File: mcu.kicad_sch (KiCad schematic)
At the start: 1 part, among them U1 STM32H747IITx

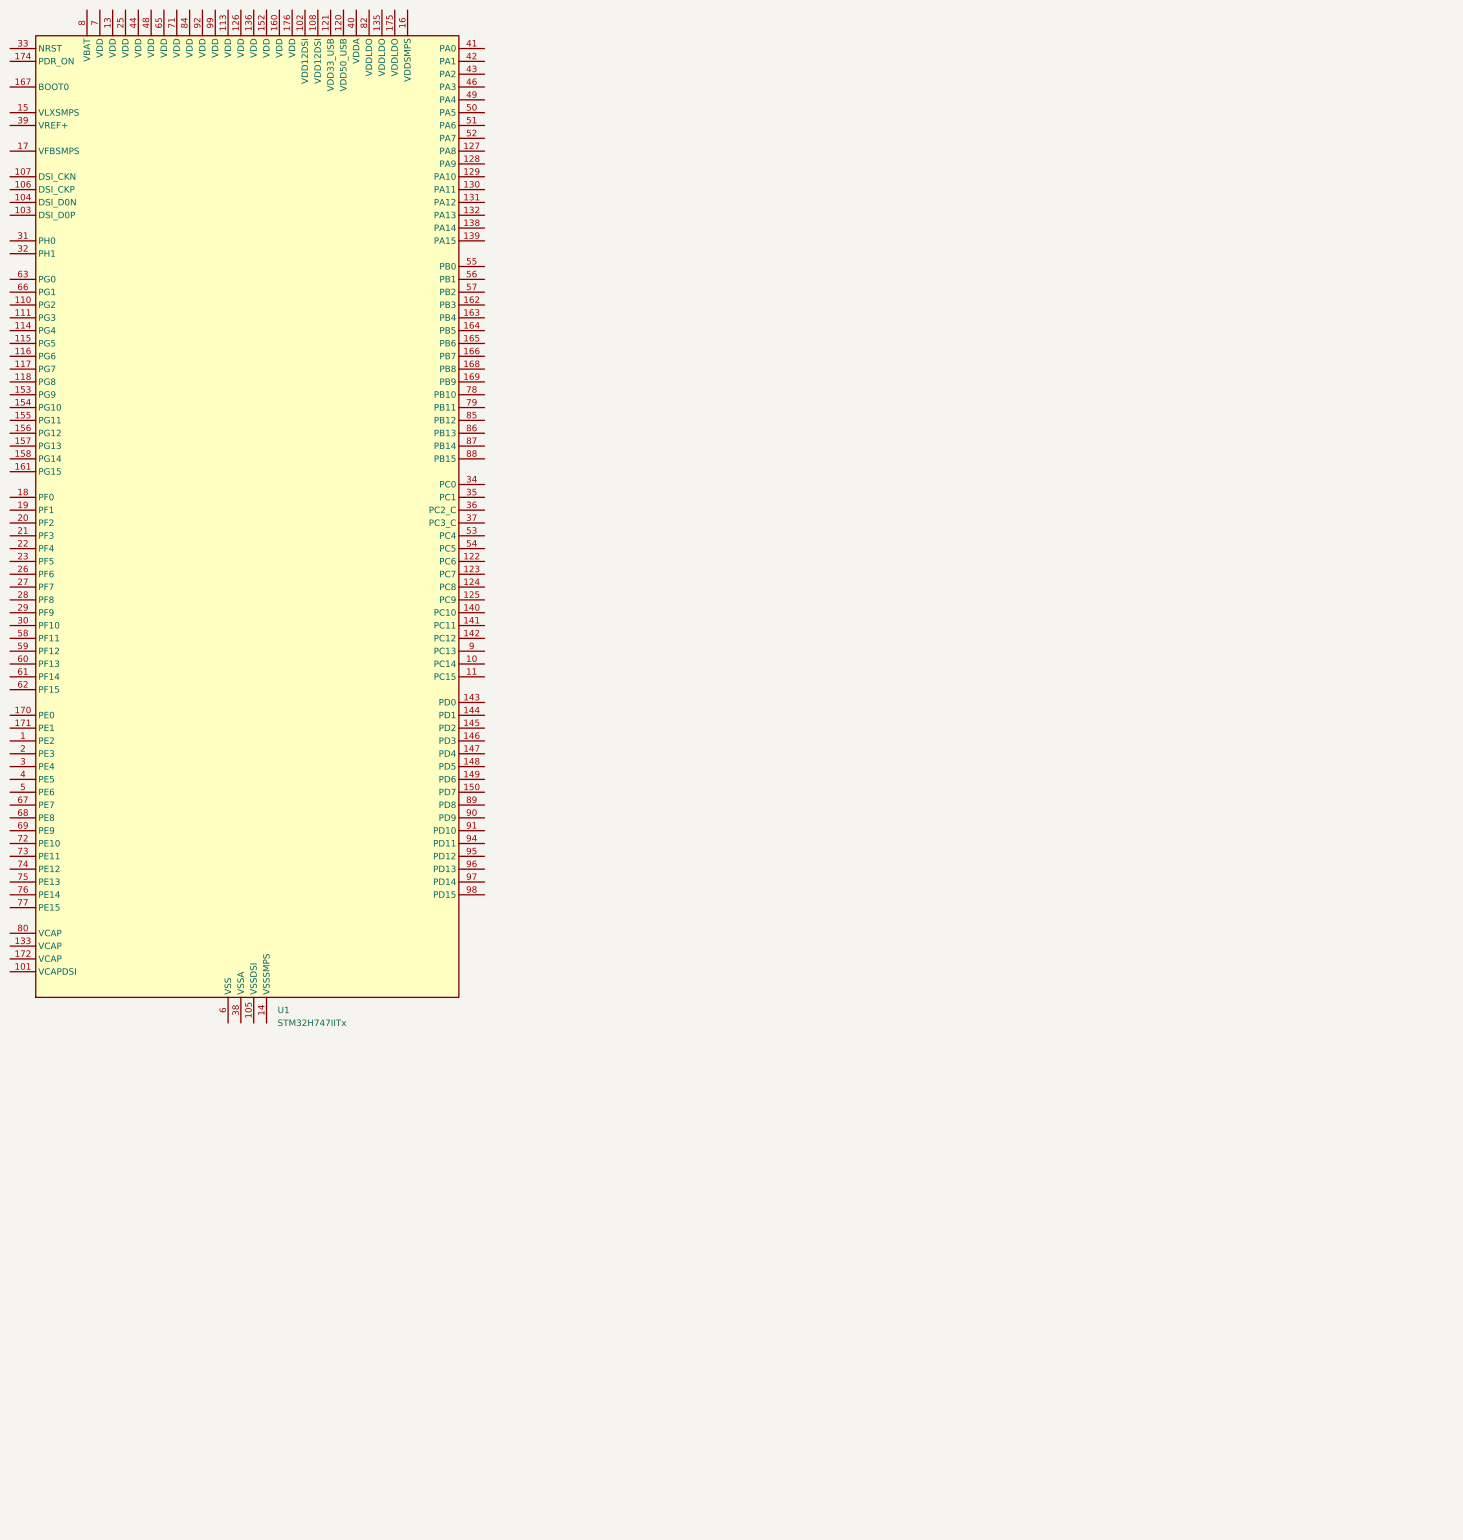
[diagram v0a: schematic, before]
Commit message: Updated processor to STM32H747XIH6
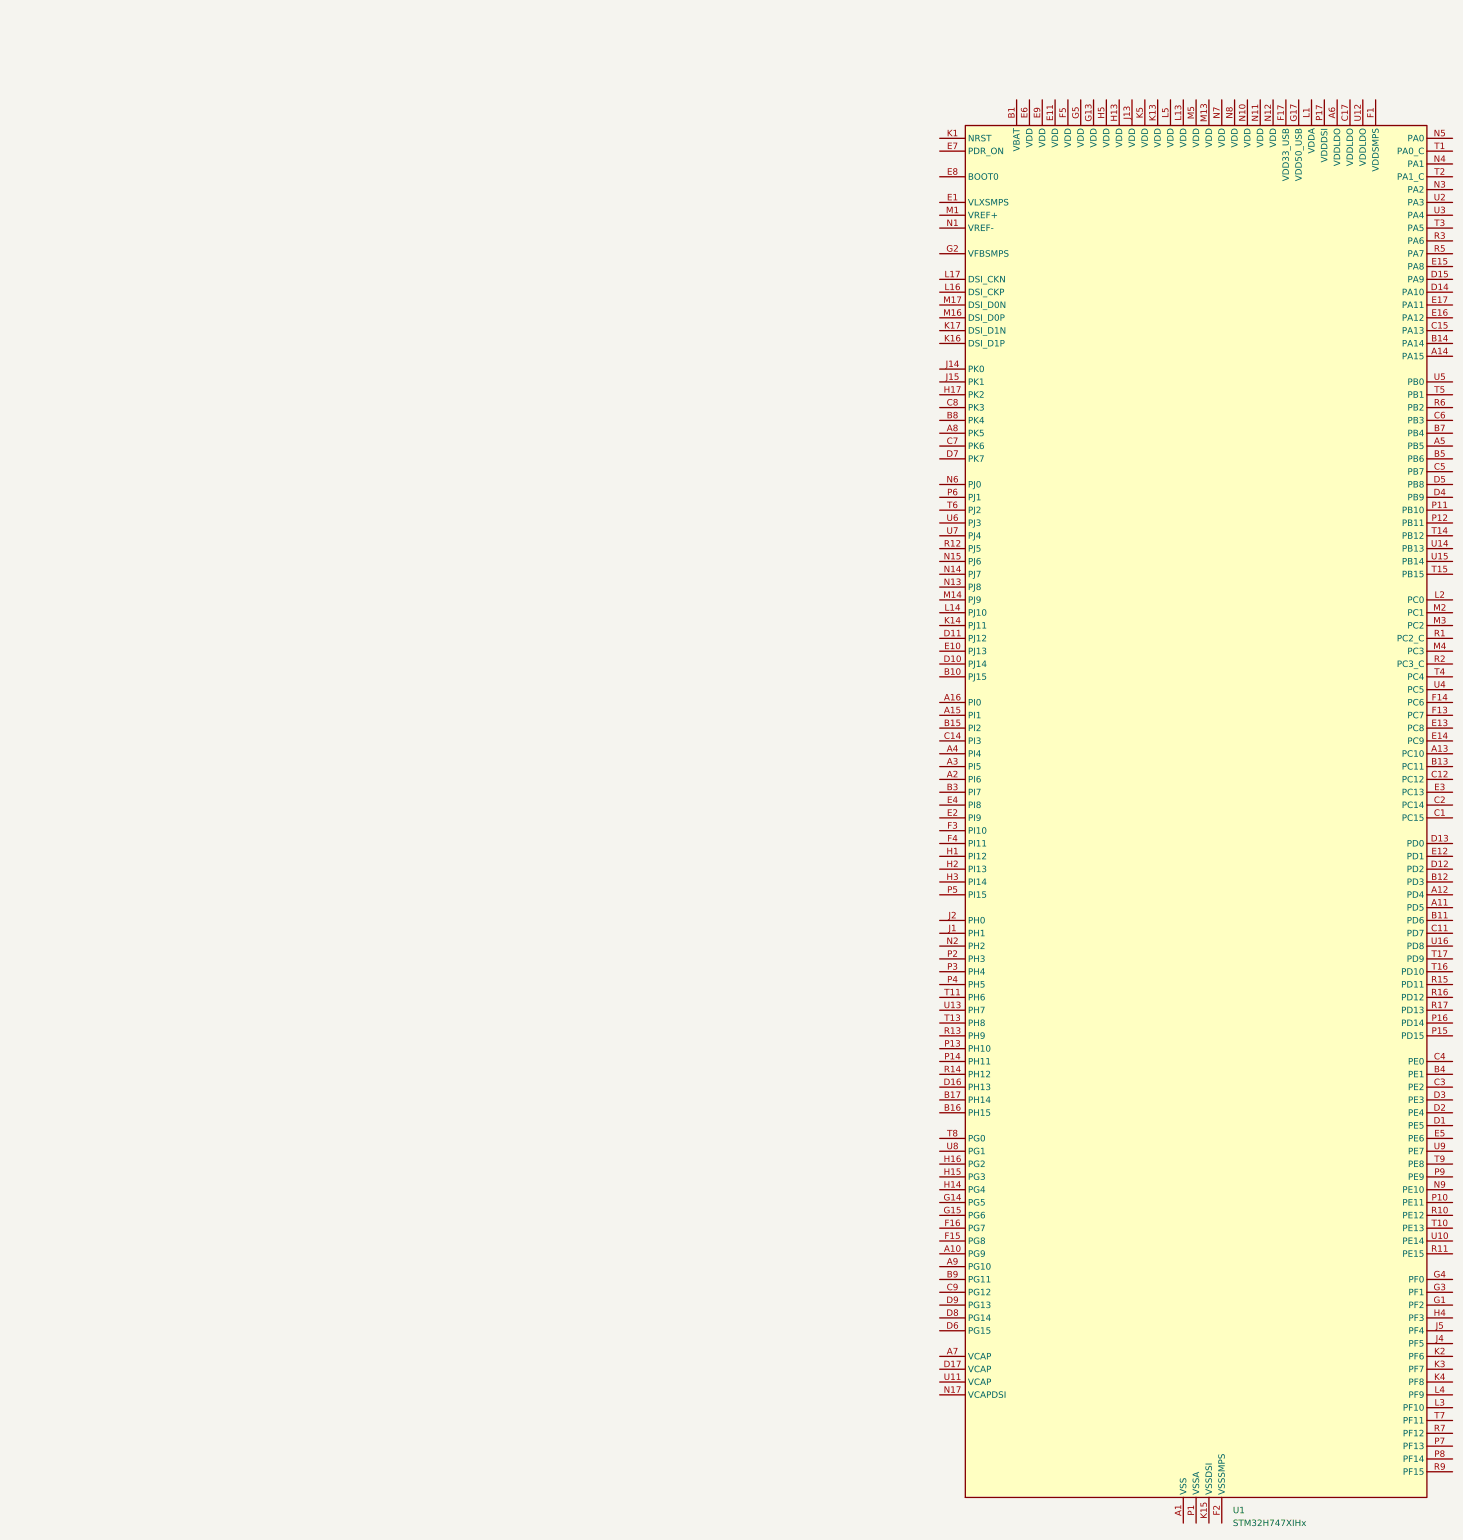
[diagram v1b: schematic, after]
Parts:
- removed U1: STM32H747IITx, Package_QFP:LQFP-176_24x24mm_P0.5mm, symbol MCU_ST_STM32H7:STM32H747IITx
- added U1: STM32H747XIHx, Package_BGA:TFBGA-265_14x14mm_Layout17x17_P0.8mm, symbol MCU_ST_STM32H7:STM32H747XIHx
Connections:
- new net: U1.A1 (VSS), U1.A17 (VSS), U1.B2 (VSS), U1.B6 (VSS), U1.C10 (VSS), U1.C13 (VSS), U1.C16 (VSS), U1.G10 (VSS), U1.G11 (VSS), U1.G16 (VSS), U1.G7 (VSS), U1.G8 (VSS), U1.G9 (VSS), U1.H10 (VSS), U1.H11 (VSS), U1.H7 (VSS), U1.H8 (VSS), U1.H9 (VSS), U1.J10 (VSS), U1.J11 (VSS), U1.J16 (VSS), U1.J17 (VSS), U1.J3 (VSS), U1.J7 (VSS), U1.J8 (VSS), U1.J9 (VSS), U1.K10 (VSS), U1.K11 (VSS), U1.K7 (VSS), U1.K8 (VSS), U1.K9 (VSS), U1.L10 (VSS), U1.L11 (VSS), U1.L7 (VSS), U1.L8 (VSS), U1.L9 (VSS), U1.N16 (VSS), U1.R4 (VSS), U1.R8 (VSS), U1.T12 (VSS), U1.U1 (VSS), U1.U17 (VSS)
- new net: U1.K15 (VSSDSI), U1.L15 (VSSDSI), U1.M15 (VSSDSI)

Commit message: Finished Layout
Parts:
- added BT1: CR2032, Battery:BatteryHolder_Keystone_1060_1x2032, symbol Device:Battery_Cell
- added C1, C10, C11, C12, C13, C14, C15, C16, C17, C18, C19, C2, C20, C22, C3, C30, C31, C32, C33, C34, C35, C36, C4, C41, C47, C48, C49, C5, C50, C54, C6, C7, C8, C9: 0.1u, Capacitor_SMD:C_0402_1005Metric, symbol Device:C
- added C21: 4.7u, Capacitor_SMD:C_0402_1005Metric, symbol Device:C
- added C23, C42: 1u, Capacitor_SMD:C_0402_1005Metric, symbol Device:C
- added C24, C28, C29: 10u, Capacitor_SMD:C_0402_1005Metric, symbol Device:C
- added C25: 220p, Capacitor_SMD:C_0402_1005Metric, symbol Device:C_Small
- added C26: 0.1u, Capacitor_SMD:C_0402_1005Metric, symbol Device:C_Small
- added C27: 1u, Capacitor_SMD:C_0402_1005Metric, symbol Device:C_Small
- added C37, C38, C39: 2.2u, Capacitor_SMD:C_0402_1005Metric, symbol Device:C
- added C43, C44, C45, C46: 12p, Capacitor_SMD:C_0402_1005Metric, symbol Device:C
- added D2: RED_LED, LED_SMD:LED_0603_1608Metric, symbol Device:LED
- added D3: GREEN_LED, LED_SMD:LED_0603_1608Metric, symbol Device:LED
- added J2: Micro_SD_Card_Det2, Connector_Card:microSD_HC_Hirose_DM3D-SF, symbol Connector:Micro_SD_Card_Det2
- added J4: RJHSE-5380-02, Connector_RJ:RJ45_Amphenol_RJHSE538X-02, symbol Connector:RJ45_LED_Shielded_x2
- added J5: Conn_01x04, Connector_Molex:Molex_Micro-Fit_3.0_43650-0400_1x04_P3.00mm_Horizontal, symbol Connector_Generic:Conn_01x04
- added L1: 2.2u, Inductor_Custom:L_0806_2016Metric, symbol Device:L
- added NT1: NetTie_2, NetTies:NetTie_2_0.25mm, symbol Device:NetTie_2
- added R1: 10k, Resistor_SMD:R_0402_1005Metric, symbol Device:R_US
- added R12, R13: 330, Resistor_SMD:R_0402_1005Metric, symbol Device:R_US
- added R5, R6: 4.7k, Resistor_SMD:R_0402_1005Metric, symbol Device:R_US
- added SW1: PTS810, Button_Switch_SMD:SW_SPST_PTS810, symbol Switch:SW_Push
- added U4: TPS22917DBV, Package_TO_SOT_SMD:SOT-23-6, symbol Power_Management:TPS22917DBV
- added U5: EMIF06-MSD02N16, ST:ST-Micro-QFN-16-1EP-2.7x0.2mm, symbol ST:EMIF06-MSD02N16
- added U6: STLINK-V3MODS, ST-Link_V3:STLink_V3MODS, symbol ST-Link_V3:STLink-V3MODS
- added U7: TJA1057GT, Package_SO:SOIC-8_3.9x4.9mm_P1.27mm, symbol Interface_CAN_LIN:MCP2562-E-SN
- added U8: SHT4x, Sensor_Humidity:Sensirion_DFN-4_1.5x1.5mm_P0.8mm_SHT4x_NoCentralPad, symbol Sensor_Humidity:SHT4x
- added U9: AS4C4M16SA, Package_BGA:Alliance_TFBGA-54_8x8mm_Layout9x9_P0.8mm, symbol Memory_Custom:AS4C4M16SA-6BIN
- added Y1: 16MHz, Crystal:Crystal_SMD_2016-4Pin_2.0x1.6mm, symbol Device:Crystal_GND24
- added Y2: Crystal, Crystal:Crystal_SMD_MicroCrystal_CM9V-T1A-2Pin_1.6x1.0mm, symbol Device:Crystal
- renumbered U1 to U2
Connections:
- net GND: now reaches U2.A1 (VSS), U2.A17 (VSS), U2.B2 (VSS), U2.B6 (VSS), U2.C10 (VSS), U2.C13 (VSS), U2.C16 (VSS), U2.G10 (VSS), U2.G11 (VSS), U2.G16 (VSS), U2.G7 (VSS), U2.G8 (VSS), U2.G9 (VSS), U2.H10 (VSS), U2.H11 (VSS), U2.H7 (VSS), U2.H8 (VSS), U2.H9 (VSS), U2.J10 (VSS), U2.J11 (VSS), U2.J16 (VSS), U2.J17 (VSS), U2.J3 (VSS), U2.J7 (VSS), U2.J8 (VSS), U2.J9 (VSS), U2.K10 (VSS), U2.K11 (VSS), U2.K7 (VSS), U2.K8 (VSS), U2.K9 (VSS), U2.L10 (VSS), U2.L11 (VSS), U2.L7 (VSS), U2.L8 (VSS), U2.L9 (VSS), U2.N16 (VSS), U2.R4 (VSS), U2.R8 (VSS), U2.T12 (VSS), U2.U1 (VSS), U2.U17 (VSS)
- net GND: now also U2.F17 (VDD33_USB), U2.F2 (VSSSMPS), U2.G17 (VDD50_USB), U2.K15 (VSSDSI), U2.L15 (VSSDSI), U2.M15 (VSSDSI), BT1.2 (-), C1.2, C10.2, C11.2, C12.2, C13.2, C14.2, C15.2, C16.2, C17.2, C18.2, C19.2, C2.2, C20.2, C21.2, C24.2, C25.2, C28.2, C29.2, C3.2, C30.2, C31.2, C32.2, C33.2, C34.2, C35.2, C36.2, C37.2, C38.2, C39.2, C4.2, C41.2, C42.2, C43.2, C44.2, C45.2, C46.2, C47.2, C48.1, C49.1, C5.2, C50.1, C54.2, C6.2, C7.2, C8.2, C9.2, D2.1 (K), D3.1 (K), J2.11 (SHIELD), J2.6 (VSS), J2.9 (DET_B), J5.4 (Pin_4), NT1.1, R1.1, SW1.1, U4.2 (GND), U5.17 (GND), U6.24 (GND), U6.26 (GND), U6.27 (GND), U6.29 (GND), U6.8 (GND), U7.2 (VSS), U7.8 (STBY), U8.4 (VSS), U9.A1 (VSS), U9.A3 (VSSQ), U9.B7 (VSSQ), U9.C3 (VSSQ), U9.D7 (VSSQ), U9.E3 (VSS), U9.J1 (VSS), Y1.2, Y1.4
- net SD_EN: now reaches U2.A11 (PD5)
- net SD_EN: now also U4.3 (ON)
- net SD_DETECT: now reaches U2.A12 (PD4)
- net SD_DETECT: now also J2.10 (DET_A), U5.1 (WP/CD)
- net SDMMC1_D2: now reaches U2.A13 (PC10)
- net SDMMC1_D2: now also U5.3 (DAT2_IN)
- net FDCAN2_RX: now reaches U2.A5 (PB5)
- net FDCAN2_RX: now also U7.4 (RXD)
- net VDDLDO: now reaches U2.A6 (VDDLDO)
- net VDDLDO: now also U2.A7 (VCAP), U2.C17 (VDDLDO), U2.D17 (VCAP), U2.G2 (VFBSMPS), U2.U11 (VCAP), U2.U12 (VDDLDO), C28.1, C29.1, C37.1, C38.1, L1.1
- net RED_LED: now reaches U2.A8 (PK5)
- net RED_LED: now also R12.1
- net +BATT: now reaches U2.B1 (VBAT)
- net +BATT: now also BT1.1 (+)
- net SDMMC1_D3: now reaches U2.B13 (PC11)
- net SDMMC1_D3: now also U5.4 (DAT3_IN)
- net SWDCLK: now reaches U2.B14 (PA14)
- net SWDCLK: now also U6.13 (JCLK/SWCLK)
- net FMC_NBL1: now reaches U2.B4 (PE1)
- net FMC_NBL1: now also U9.F1 (UDQM)
- net FDCAN2_TX: now reaches U2.B5 (PB6)
- net FDCAN2_TX: now also U7.1 (TXD)
- net RADIO_RX: now reaches U2.B7 (PB4)
- net RADIO_RX: now also J5.3 (Pin_3)
- net GREEN_LED: now reaches U2.B8 (PK4)
- net GREEN_LED: now also R13.1
- net LSE_OUT: now reaches U2.C1 (PC15)
- net LSE_OUT: now also C46.1, Y2.2
- net SDMMC1_CK: now reaches U2.C12 (PC12)
- net SDMMC1_CK: now also U5.6 (CLK_IN)
- net SWDIO: now reaches U2.C15 (PA13)
- net SWDIO: now also U6.4 (JTMS/SWDIO)
- net LSE_IN: now reaches U2.C2 (PC14)
- net LSE_IN: now also C45.1, Y2.1
- net FMC_NBL0: now reaches U2.C4 (PE0)
- net FMC_NBL0: now also U9.E8 (LDQM)
- net RADIO_TX: now reaches U2.C6 (PB3)
- net RADIO_TX: now also J5.2 (Pin_2)
- net GPS_TIMEPULSE: now reaches U2.D1 (PE5)
- net SDMMC1_CMD: now reaches U2.D12 (PD2)
- net SDMMC1_CMD: now also U5.5 (CMD_IN)
- net FMC_D2: now reaches U2.D13 (PD0)
- net FMC_D2: now also U9.B8 (DQ2)
- net USART1_RX: now reaches U2.D14 (PA10)
- net USART1_RX: now also U6.15 (VCP_RX)
- net USART1_TX: now reaches U2.D15 (PA9)
- net USART1_TX: now also U6.12 (VCP_TX)
- net GPS_EXTINT: now reaches U2.D2 (PE4)
- net GPS_~{RESET}: now reaches U2.D3 (PE3)
- net FMC_SDNCAS: now reaches U2.D6 (PG15)
- net FMC_SDNCAS: now also U9.F7 (~{CAS})
- net at U2.E1 (VLXSMPS): now also C25.1, L1.2
- net +3.3V: now reaches U2.E11 (VDD)
- net +3.3V: now also U2.E6 (VDD), U2.E7 (PDR_ON), U2.E9 (VDD), U2.F1 (VDDSMPS), U2.F5 (VDD), U2.G13 (VDD), U2.G5 (VDD), U2.H13 (VDD), U2.H5 (VDD), U2.J13 (VDD), U2.K13 (VDD), U2.K5 (VDD), U2.L1 (VDDA), U2.L13 (VDD), U2.L5 (VDD), U2.M1 (VREF+), U2.M13 (VDD), U2.M5 (VDD), U2.N10 (VDD), U2.N11 (VDD), U2.N12 (VDD), U2.N7 (VDD), U2.N8 (VDD), U2.P17 (VDDDSI), C1.1, C10.1, C11.1, C12.1, C13.1, C14.1, C15.1, C16.1, C17.1, C18.1, C19.1, C2.1, C20.1, C21.1, C22.1, C23.1, C24.1, C26.1, C27.1, C3.1, C30.1, C31.1, C32.1, C33.1, C34.1, C35.1, C36.1, C4.1, C42.1, C49.2, C5.1, C50.2, C54.1, C6.1, C7.1, C8.1, C9.1, R5.1, R6.1, U4.1 (VIN), U5.15 (VCC), U5.16 (RDATA_VCC), U6.30 (VCC), U7.5 (Vio), U8.3 (VDD), U9.A7 (VDDQ), U9.A9 (VDD), U9.B3 (VDDQ), U9.C7 (VDDQ), U9.D3 (VDDQ), U9.E7 (VDD), U9.J9 (VDD)
- net FMC_D3: now reaches U2.E12 (PD1)
- net FMC_D3: now also U9.C9 (DQ3)
- net SDMMC1_D0: now reaches U2.E13 (PC8)
- net SDMMC1_D0: now also U5.7 (DAT0_IN)
- net SDMMC1_D1: now reaches U2.E14 (PC9)
- net SDMMC1_D1: now also U5.8 (DAT1_IN)
- net GPS_~{SAFEBOOT}: now reaches U2.E2 (PI9)
- net at U2.E8 (BOOT0): now also R1.2
- net FMC_SDCLK: now reaches U2.F15 (PG8)
- net FMC_SDCLK: now also U9.F2 (CLK)
- net FMC_A2: now reaches U2.G1 (PF2)
- net FMC_A2: now also U9.J8 (A2)
- net FMC_BA1: now reaches U2.G14 (PG5)
- net FMC_BA1: now also U9.G8 (BA1)
- net FMC_A1: now reaches U2.G3 (PF1)
- net FMC_A1: now also U9.H8 (A1)
- net FMC_A0: now reaches U2.G4 (PF0)
- net FMC_A0: now also U9.H7 (A0)
- net FMC_BA0: now reaches U2.H14 (PG4)
- net FMC_BA0: now also U9.G7 (BA0)
- net DISPLAY_~{RESET}: now reaches U2.H16 (PG2)
- net DISPLAY_TE: now reaches U2.H17 (PK2)
- net FMC_A3: now reaches U2.H4 (PF3)
- net FMC_A3: now also U9.J7 (A3)
- net HSE_OUT: now reaches U2.J1 (PH1)
- net HSE_OUT: now also C44.1, Y1.3
- net BL_PWM: now reaches U2.J15 (PK1)
- net HSE_IN: now reaches U2.J2 (PH0)
- net HSE_IN: now also C43.1, Y1.1
- net FMC_A5: now reaches U2.J4 (PF5)
- net FMC_A5: now also U9.J2 (A5)
- net FMC_A4: now reaches U2.J5 (PF4)
- net FMC_A4: now also U9.J3 (A4)
- net NRST: now reaches U2.K1 (NRST)
- net NRST: now also C47.1, SW1.2, U6.31 (NRST)
- net DSI_DSI1P: now reaches U2.K16 (DSI_D1P)
- net DSI_DSI1N: now reaches U2.K17 (DSI_D1N)
- net DSI_CLKP: now reaches U2.L16 (DSI_CKP)
- net DSI_CLKN: now reaches U2.L17 (DSI_CKN)
- net DSI_DSI0P: now reaches U2.M16 (DSI_D0P)
- net DSI_DSI0N: now reaches U2.M17 (DSI_D0N)
- net VSSA: now reaches U2.N1 (VREF-)
- net VSSA: now also U2.P1 (VSSA), C22.2, C23.2, C26.2, C27.2, NT1.2
- net VCAPDSI: now reaches U2.N17 (VCAPDSI)
- net VCAPDSI: now also C39.1
- net FMC_D7: now reaches U2.N9 (PE10)
- net FMC_D7: now also U9.E9 (DQ7)
- net FMC_D8: now reaches U2.P10 (PE11)
- net FMC_D8: now also U9.E1 (DQ8)
- net FMC_D1: now reaches U2.P15 (PD15)
- net FMC_D1: now also U9.B9 (DQ1)
- net FMC_D0: now reaches U2.P16 (PD14)
- net FMC_D0: now also U9.A8 (DQ0)
- net FMC_A7: now reaches U2.P7 (PF13)
- net FMC_A7: now also U9.H2 (A7)
- net FMC_A8: now reaches U2.P8 (PF14)
- net FMC_A8: now also U9.H1 (A8)
- net FMC_D6: now reaches U2.P9 (PE9)
- net FMC_D6: now also U9.D8 (DQ6)
- net ADC3_IN0: now reaches U2.R1 (PC2_C)
- net FMC_D9: now reaches U2.R10 (PE12)
- net FMC_D9: now also U9.D2 (DQ9)
- net FMC_D12: now reaches U2.R11 (PE15)
- net FMC_D12: now also U9.C1 (DQ12)
- net I2C4_SCL: now reaches U2.R16 (PD12)
- net I2C4_SCL: now also R5.2, U8.2 (SCL)
- net I2C4_SDA: now reaches U2.R17 (PD13)
- net I2C4_SDA: now also R6.2, U8.1 (SDA)
- net FMC_SDNWE: now reaches U2.R5 (PA7)
- net FMC_SDNWE: now also U9.F9 (~{WE})
- net FMC_A6: now reaches U2.R7 (PF12)
- net FMC_A6: now also U9.H3 (A6)
- net FMC_A9: now reaches U2.R9 (PF15)
- net FMC_A9: now also U9.G3 (A9)
- net GPS_TX: now reaches U2.T1 (PA0_C)
- net FMC_D10: now reaches U2.T10 (PE13)
- net FMC_D10: now also U9.D1 (DQ10)
- net FMC_D15: now reaches U2.T16 (PD10)
- net FMC_D15: now also U9.A2 (DQ15)
- net FMC_D14: now reaches U2.T17 (PD9)
- net FMC_D14: now also U9.B1 (DQ14)
- net GPS_RX: now reaches U2.T2 (PA1_C)
- net FMC_SDNE0: now reaches U2.T4 (PC4)
- net FMC_SDNE0: now also U9.G9 (~{CS})
- net FMC_SDNRAS: now reaches U2.T7 (PF11)
- net FMC_SDNRAS: now also U9.F8 (~{RAS})
- net FMC_A10: now reaches U2.T8 (PG0)
- net FMC_A10: now also U9.H9 (A10)
- net FMC_D5: now reaches U2.T9 (PE8)
- net FMC_D5: now also U9.D9 (DQ5)
- net FMC_D11: now reaches U2.U10 (PE14)
- net FMC_D11: now also U9.C2 (DQ11)
- net FMC_D13: now reaches U2.U16 (PD8)
- net FMC_D13: now also U9.B2 (DQ13)
- net FMC_SDCKE0: now reaches U2.U4 (PC5)
- net FMC_SDCKE0: now also U9.F3 (CKE)
- net FMC_A11: now reaches U2.U8 (PG1)
- net FMC_A11: now also U9.G2 (A11)
- net FMC_D4: now reaches U2.U9 (PE7)
- net FMC_D4: now also U9.C8 (DQ4)
- new net: D2.2 (A), R12.2
- new net: J2.1 (DAT2), U5.14 (DAT2_EX)
- new net: J2.2 (DAT3/CD), U5.13 (DAT3_EX)
- new net: J2.3 (CMD), U5.12 (CMD_EX)
- new net: J2.5 (CLK), U5.11 (CLK_EX)
- new net: J2.7 (DAT0), U5.10 (DAT0_EX)
- new net: J2.8 (DAT1), U5.9 (DAT1_EX)
- new net: J4.1, J4.13
- new net: J4.14, J4.2
- new net: J4.16, J4.4
- new net: J4.17, J4.5
- new net: J4.19, J4.7
- new net: J4.20, J4.8
- new net: J4.SH, J4.SH
- new net: D3.2 (A), R13.2
- new net: U9.E2 (NC), U9.G1 (NC)
- new net +5V: C48.2, J5.1 (Pin_1), U7.3 (VDD)
- new net CANH: J4.15, J4.3, U7.7 (CANH)
- new net CANL: J4.18, J4.6, U7.6 (CANL)
- new net SD_VDD: C41.1, J2.4 (VDD), U4.5 (QOD), U4.6 (VOUT)
- no-connect marks 0 -> 2
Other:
- note added: "Uses Direct SMPS Supply Topology"

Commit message: Minor edits to layout. Added extra models.
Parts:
- added C51, C52: 22p, Capacitor_SMD:C_0402_1005Metric, symbol Device:C
- added C68: 0.1u, Capacitor_SMD:C_0402_1005Metric, symbol Device:C
- added D3: PESD1CAN, Package_TO_SOT_SMD:SOT-23, symbol Diode:SM712_SOT23
- added FB1: 10ohm/1A, Inductor_SMD:L_0402_1005Metric, symbol Device:FerriteBead_Small
- J4: renamed from J5; value Conn_01x04 -> 043650-0401
- renumbered C1 to C10, C2 to C11, C3 to C12, C4 to C13, C5 to C14, C6 to C15, C7 to C16, C8 to C17, C9 to C18, C10 to C19, C11 to C20, C12 to C21, C13 to C22, C14 to C23, C15 to C24, C16 to C25, C17 to C26, C18 to C27, C19 to C28, C20 to C29, C21 to C30, C22 to C31, C23 to C32, C24 to C33, C54 to C34, C47 to C35, C25 to C36, C26 to C37, C27 to C38, C28 to C39, C29 to C40, C42 to C41, C41 to C42, C48 to C43, C30 to C44, C31 to C45, C32 to C46, C33 to C47, C34 to C48, C35 to C49, C36 to C50, C49 to C53, C50 to C54, C43 to C55, C44 to C56, C45 to C57, C46 to C58, C37 to C59, C38 to C60, C39 to C61, D3 to D1, J4 to J3, L1 to L3, NT1 to NT2, R1 to R5, R13 to R6, R12 to R7, R5 to R8, R6 to R9, U6 to U2, U5 to U3, U7 to U5, U9 to U6, U2 to U7
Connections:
- net +3.3V: now also FB1.1; no longer C44.1, C45.1, C46.1, C47.1, C48.1, C49.1, C50.1, U6.A7 (VDDQ), U6.A9 (VDD), U6.B3 (VDDQ), U6.C7 (VDDQ), U6.D3 (VDDQ), U6.E7 (VDD), U6.J9 (VDD)
- net +BATT: now also C68.1
- net CANH: now also C51.2, D3.2 (A2)
- net CANL: now also C52.1, D3.1 (A1)
- net GND: now also C51.1, C52.2, C68.2, D3.3 (common)
- net SD_DETECT: now also U7.B12 (PD3); no longer U7.A12 (PD4)
- net GPS_EN: now reaches U7.U2 (PA3)
- new net RAM_VDD: C44.1, C45.1, C46.1, C47.1, C48.1, C49.1, C50.1, FB1.2, U6.A7 (VDDQ), U6.A9 (VDD), U6.B3 (VDDQ), U6.C7 (VDDQ), U6.D3 (VDDQ), U6.E7 (VDD), U6.J9 (VDD)
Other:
- moved on the sheet: BT1, C43, C53, U5
